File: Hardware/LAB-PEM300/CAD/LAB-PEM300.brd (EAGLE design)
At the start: 160 x 100 mm, 4 parts, among them IC1 AD7992, IC2 TPS77028

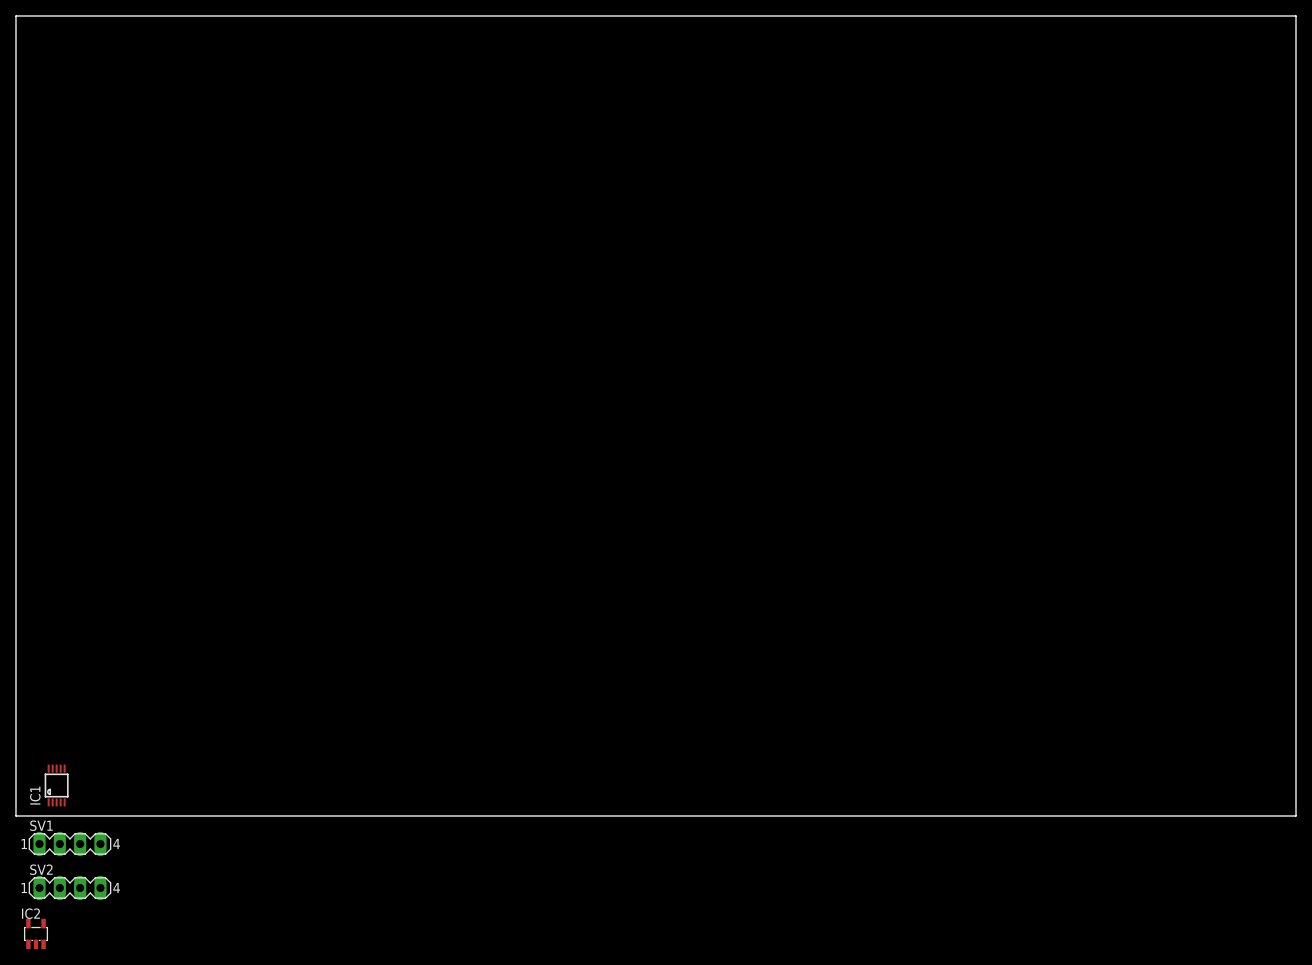
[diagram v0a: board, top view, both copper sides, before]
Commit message: Completed LAB-PEM300 Design, Layout, BOM
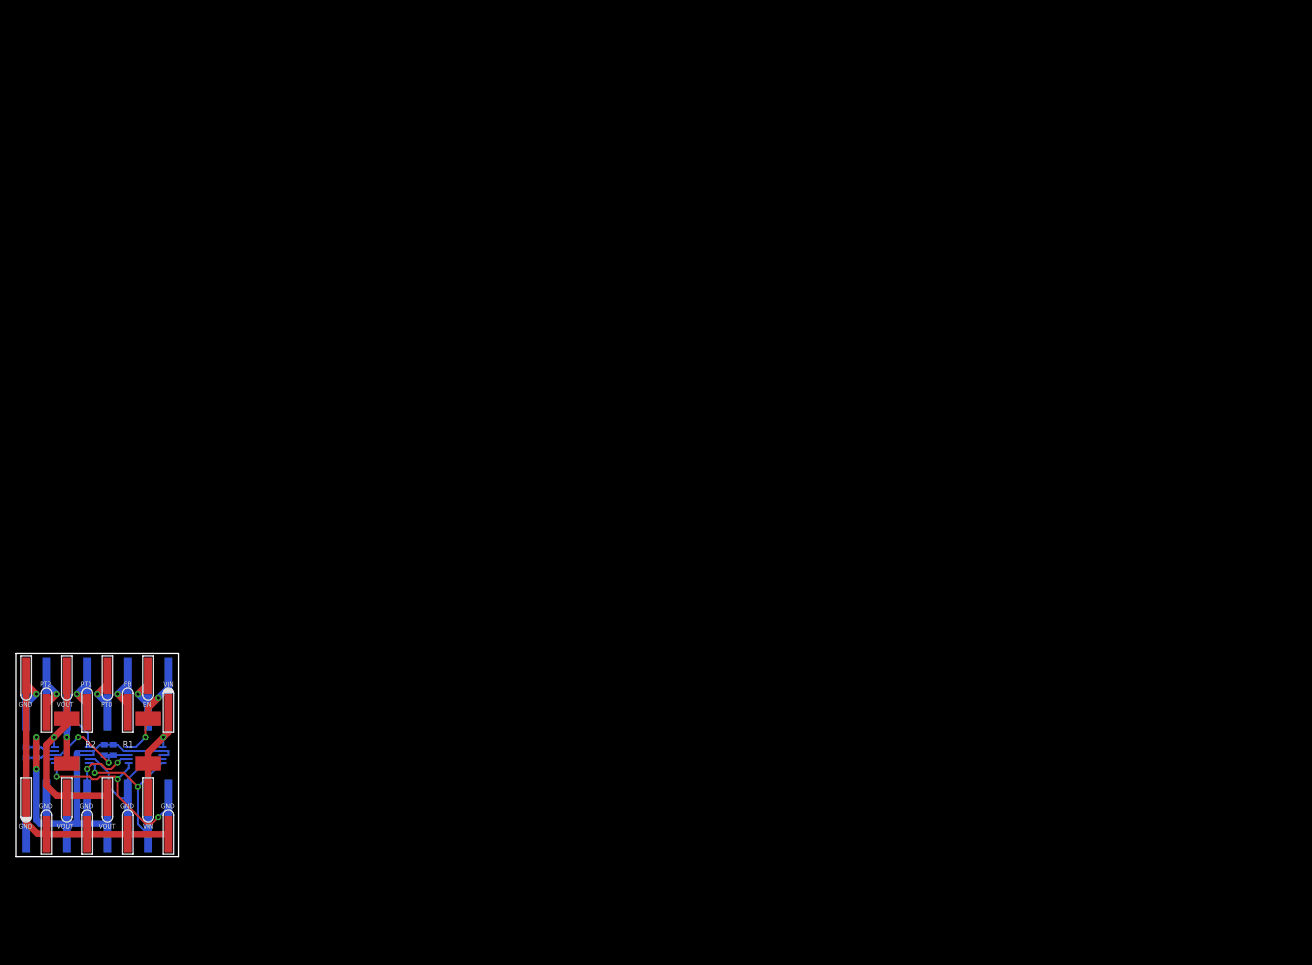
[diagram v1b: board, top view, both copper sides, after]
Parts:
- removed IC1: AD7992, analog-devices:MSOP10
- removed IC2: TPS77028, texas:SOT23-DBV
- removed SV1, SV2: (no value), con-lstb:MA04-1
- added C1, C3: .1uF, rcl:C0402
- added C2, C4: 10uF, rcl:C0402
- added J1, J2: SULLINSSMTPINHEADER-8, LAB-PEM300:SMTHEADER-8
- added J3, J4: (no value), LAB-PEM300:SMTHEADER-8
- added R1, R2: 1, rcl:R2512
- added U1, U2: AD8253, LAB-PEM300:MSOP10
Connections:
- removed net AGND: IC1.2, IC1.7
- removed net GND: IC2.2
- removed net VDD: IC1.3
- new net !AN_WR: J2.P$8, U1.6, U2.6
- new net AN_A0: J2.P$6, U1.4, U2.4
- new net AN_A1: J2.P$7, U1.5, U2.5
- new net AN_GND: C1.2, C2.2, C3.2, C4.2, J2.P$3, J2.P$5, U1.2, U1.3, U1.9, U2.2, U2.3, U2.9
- new net AN_IIN: J2.P$4, U2.7
- new net AN_IOUT: J2.P$2, U1.7
- new net AN_VIN: C1.1, C2.1, C3.1, C4.1, J2.P$1, U1.8, U2.8
- new net BRD_VIN: J1.P$1, R1.1, U2.10
- new net BRD_VOUT: J1.P$6, R2.1, U1.1
- new net PSU_EN: J1.P$2, J3.P$2
- new net PSU_FB: J1.P$3, J3.P$3
- new net PSU_GND: J1.P$8, J3.P$8, J4.P$1, J4.P$2, J4.P$4, J4.P$6, J4.P$8
- new net PSU_PT0: J1.P$4, J3.P$4
- new net PSU_PT1: J1.P$5, J3.P$5
- new net PSU_PT2: J1.P$7, J3.P$7
- new net PSU_VIN: J3.P$1, J4.P$7, R1.2, U2.1
- new net PSU_VOUT: J3.P$6, J4.P$3, J4.P$5, R2.2, U1.10
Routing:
- net AN_GND: track 0.00 -> 52.1 mm, vias 0 -> 2
- net PSU_GND: track 0.00 -> 41.4 mm, vias 0 -> 1
- net AN_VIN: track 0.00 -> 26.9 mm, vias 0 -> 2
- net PSU_VOUT: track 0.00 -> 24.9 mm, vias 0 -> 1
- net !AN_WR: track 0.00 -> 24.4 mm, vias 0 -> 3
- net AN_A1: track 0.00 -> 18.9 mm, vias 0 -> 2
- net AN_A0: track 0.00 -> 15.6 mm
- net PSU_VIN: track 0.00 -> 13.1 mm, vias 0 -> 1
- net BRD_VOUT: track 0.00 -> 12.6 mm, vias 0 -> 1
- net BRD_VIN: track 0.00 -> 11.5 mm, vias 0 -> 2
- net AN_IIN: track 0.00 -> 9.82 mm, vias 0 -> 2
- net AN_IOUT: track 0.00 -> 5.63 mm
- net PSU_FB: track 0.00 -> 5.62 mm, vias 0 -> 1
- net PSU_EN: track 0.00 -> 5.62 mm, vias 0 -> 1
- net PSU_PT2: track 0.00 -> 5.62 mm, vias 0 -> 1
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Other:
- board size 160 x 100 mm -> 20.3 x 25.4 mm
- board text added: "!WR"
- board text added: "A0"
- board text added: "A1"
- board text added: "AGND"
- board text added: "AVIN"
- board text added: "EN"
- board text added: "FB"
- board text added: "GND"
- board text added: "IIN"
- board text added: "IOUT"
- board text added: "J1"
- board text added: "J2"
- board text added: "PT0"
- board text added: "PT1"
- board text added: "PT2"
- board text added: "VIN"
- board text added: "VOUT"
